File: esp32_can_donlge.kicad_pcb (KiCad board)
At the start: 4 copper layers, 86 parts, among them J1 Conn_01x02_Male, J2 DM3AT-SF-PEJM5(40), J3 DB9_Male, J4 USB_B_Micro, Q1 DMG2305UX-7, Q2 BC817, Q3 BC817, U1 ESP32-WROOM-32, U2 SN65HVD230DR, U3 TLP175A, U4 LT8607, U5 USBLC6-2SC6, U6 CP2102N-A01-GQFN24, Y1 LFXTAL009709Bulk

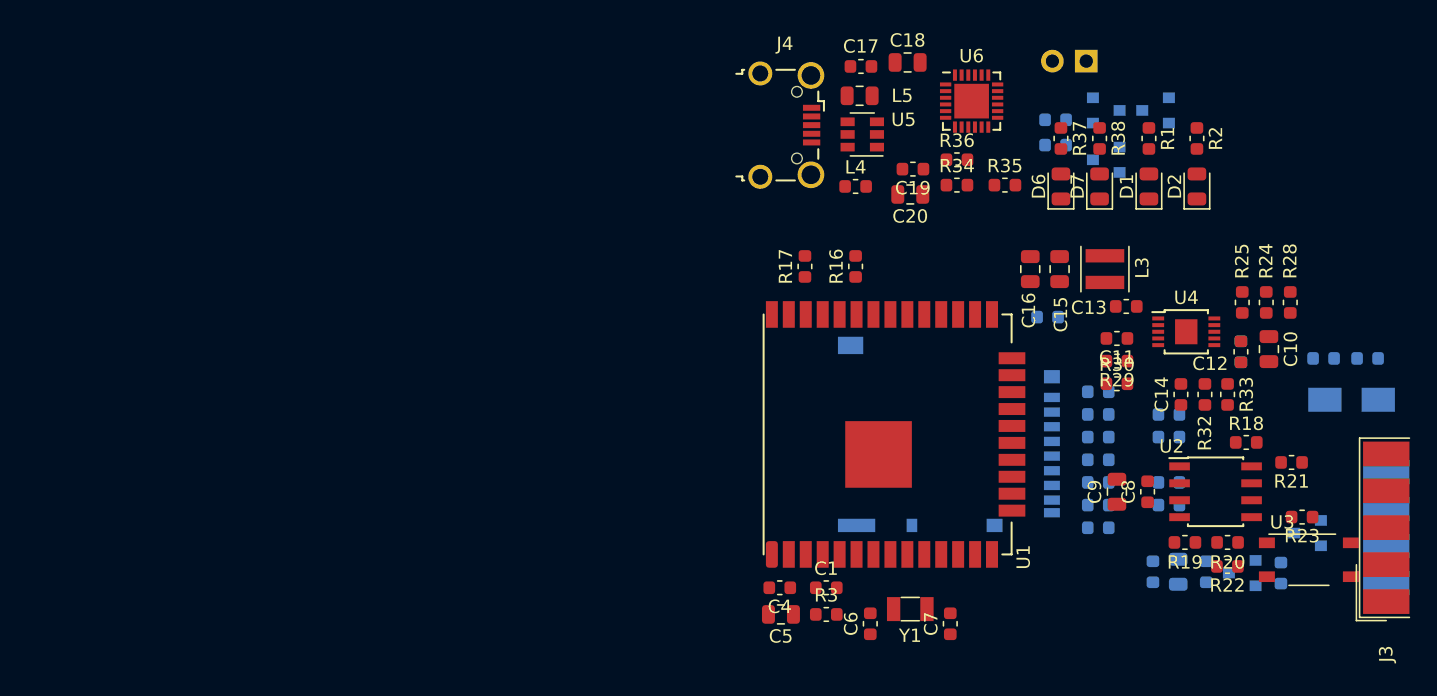
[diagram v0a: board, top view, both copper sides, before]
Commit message: changed to a more basic variant of the esp32
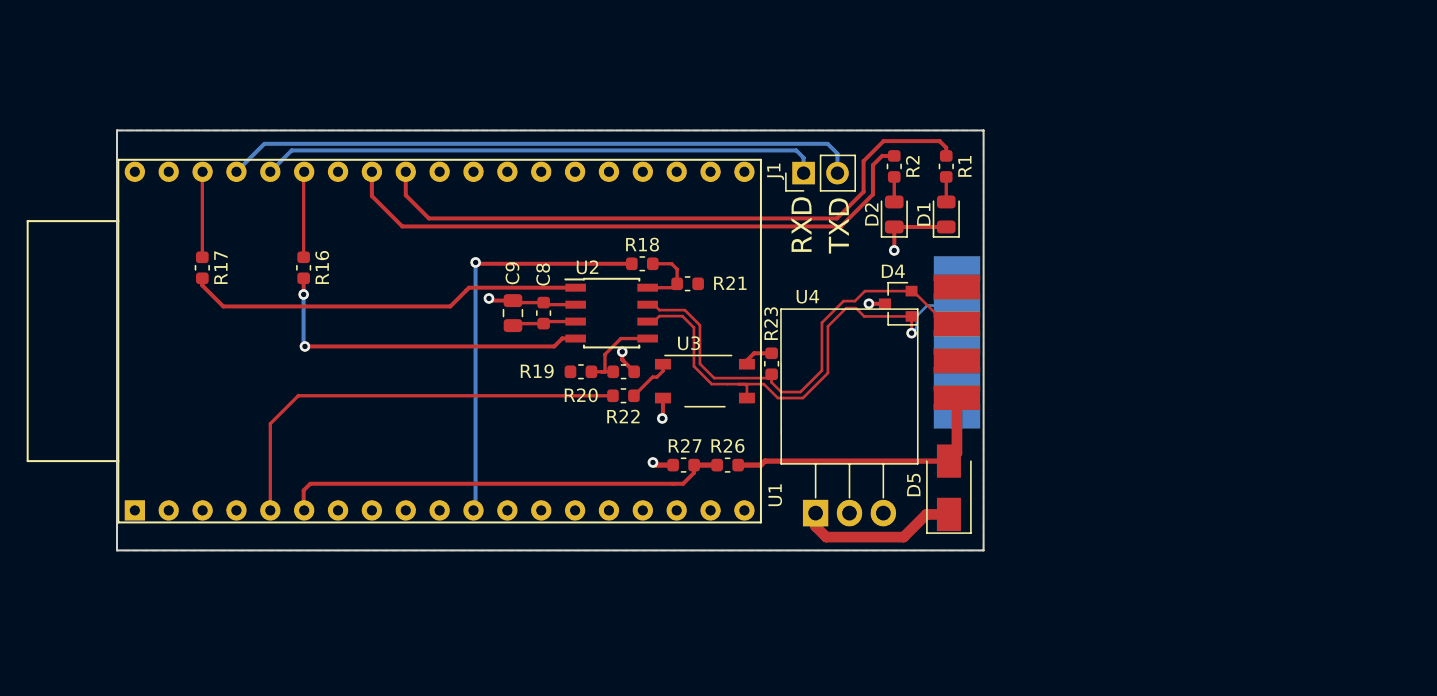
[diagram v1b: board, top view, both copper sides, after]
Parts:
- removed C1, C13, C19, C2, C4: 100n/25V, bytewerk_capacitors:C_0603_1608Metric
- removed C10, C15, C16, C3, C5: 10u/25V, bytewerk_capacitors:C_0805_2012Metric
- removed C11: 1u/25V, bytewerk_capacitors:C_0603_1608Metric
- removed C12: 10n/25V, bytewerk_capacitors:C_0603_1608Metric
- removed C14: 10p/50V, bytewerk_capacitors:C_0603_1608Metric
- removed C17: 100n/10V, bytewerk_capacitors:C_0603_1608Metric
- removed C18, C20: 4u7/10V, bytewerk_capacitors:C_0805_2012Metric
- removed C6, C7: C, bytewerk_capacitors:C_0603_1608Metric
- removed D3: BAT54C, Package_TO_SOT_SMD:SOT-23
- removed D6, D7: LED, LED_SMD:LED_0805_2012Metric
- removed J2: DM3AT-SF-PEJM5(40), Connector_Card:microSD_HC_Hirose_DM3AT-SF-PEJM5
- removed J4: USB_B_Micro, Connector_USB:USB_Micro-B_Wuerth_629105150521_CircularHoles
- removed L1, L2, L4: L, Inductor_SMD:L_0603_1608Metric
- removed L3: XFL3012-222ME, bytewerk-inductors:L_Coilcraft_XLF3012
- removed L5: L, Inductor_SMD:L_0805_2012Metric
- removed Q1: DMG2305UX-7, Package_TO_SOT_SMD:SOT-23
- removed Q2, Q3: BC817, Package_TO_SOT_SMD:SOT-23
- removed R10: 10R, bytewerk_resistors:R_0603_1608Metric
- removed R11, R12, R13, R9: 33R, bytewerk_resistors:R_0603_1608Metric
- removed R14, R30: 200R, bytewerk_resistors:R_0603_1608Metric
- removed R15, R3, R4, R5, R6, R7, R8: 10k, bytewerk_resistors:R_0603_1608Metric
- removed R24, R32: 1M, bytewerk_resistors:R_0603_1608Metric
- removed R25: 120k, bytewerk_resistors:R_0603_1608Metric
- removed R28: n.b., bytewerk_resistors:R_0603_1608Metric
- removed R29: 18k, bytewerk_resistors:R_0603_1608Metric
- removed R31: 82k, bytewerk_resistors:R_0603_1608Metric
- removed R33: 309k, bytewerk_resistors:R_0603_1608Metric
- removed R34: 22k, bytewerk_resistors:R_0603_1608Metric
- removed R35: 47k, bytewerk_resistors:R_0603_1608Metric
- removed R36, R37, R38, R39, R40: 1k, bytewerk_resistors:R_0603_1608Metric
- removed U5: USBLC6-2SC6, Package_TO_SOT_SMD:SOT-23-6
- removed U6: CP2102N-A01-GQFN24, Package_DFN_QFN:QFN-24-1EP_4x4mm_P0.5mm_EP2.6x2.6mm
- removed Y1: LFXTAL009709Bulk, Crystal:Crystal_SMD_3215-2Pin_3.2x1.5mm
- D4, D5, R26, R27: moved to F.Cu
- J1: footprint Connector_PinHeader_2.54mm:PinHeader_1x02_P2.54mm_Horizontal -> Connector_PinHeader_2.54mm:PinHeader_1x02_P2.54mm_Vertical; moved to F.Cu
- J3: moved to B.Cu
- U1: value ESP32-WROOM-32 -> ESP32-DevKitC-32D; footprint bytewerk-esp32:ESP32-WROOM-32 -> bytewerk-esp32:ESP32-DevKitC-32D
- U4: value LT8607 -> OKI-78SR; footprint Package_SO:MSOP-10-1EP_3x3mm_P0.5mm_EP1.68x1.88mm -> bytewerk-TO-packages:TO-220-3_Horizontal_TabDown
- moved R26 48.7 mm to (157.0, 94.6)
- moved R27 48.7 mm to (153.7, 94.6)
- moved R18 47.2 mm to (150.6, 79.5)
- moved R21 47.2 mm to (154.0, 81.0)
- moved C8 47.2 mm to (143.2, 83.2)
- moved U3 47.2 mm to (155.3, 88.3)
- moved C9 47.2 mm to (140.9, 83.2)
- moved U2 47.2 mm to (148.3, 83.2)
- moved R19 47.1 mm to (146.0, 87.6)
- moved R20 47.1 mm to (149.2, 87.6)
- moved R22 47.1 mm to (149.2, 89.4)
- moved R17 45.2 mm to (117.6, 79.8), turned to 270 degrees
- moved R23 41.4 mm to (160.3, 87.0), turned to 90 degrees
- moved R16 41.4 mm to (125.2, 79.8), turned to 270 degrees
- moved D4 35.2 mm to (169.8, 82.5)
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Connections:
- J1 pad 1: /esp32/BOOT -> /esp32/RXD
- J1 pad 2: GND -> /esp32/TXD
- U1 pad 1: GND -> +3V3
- U1 pad 10: /esp32/DET_B -> (no net)
- U1 pad 11: /esp32/SD_EN -> /can_interface/CAN_EN
- U1 pad 12: /can_interface/CAN_EN -> (no net)
- U1 pad 13: /esp32/SD_CLK -> (no net)
- U1 pad 14: /esp32/SD_DAT2 -> GND
- U1 pad 15: GND -> (no net)
- U1 pad 16: /esp32/SD_DAT3 -> (no net)
- U1 pad 2: +3V3 -> (no net)
- U1 pad 20: (no net) -> GND
- U1 pad 22: (no net) -> Net-(R17-Pad1)
- U1 pad 23: /esp32/SD_CMD -> /esp32/TXD
- U1 pad 24: /esp32/SD_DAT0 -> /esp32/RXD
- U1 pad 25: /esp32/BOOT -> Net-(R16-Pad1)
- U1 pad 26: /esp32/SD_DAT1 -> GND
- U1 pad 27: /esp32/DET_A -> /esp32/TEST_LED1
- U1 pad 28: /esp32/DET_B -> /esp32/TEST_LED0
- U1 pad 3: /esp32/ESP_EN -> (no net)
- U1 pad 30: /esp32/TEST_LED0 -> (no net)
- U1 pad 31: /esp32/TEST_LED1 -> (no net)
- U1 pad 33: Net-(R16-Pad1) -> (no net)
- U1 pad 34: /usb_uart/TXD -> (no net)
- U1 pad 35: /usb_uart/RXD -> (no net)
- U1 pad 36: Net-(R17-Pad1) -> (no net)
- U1 pad 37: /esp32/DET_A -> (no net)
- U1 pad 38: GND -> (no net)
- U1 pad 5: (no net) -> /can_interface/CAN_TERM_EN
- U1 pad 6: /can_interface/CAN_TERM_EN -> BAT_ADC_IN
- U1 pad 7: BAT_ADC_IN -> (no net)
- U1 pad 8: Net-(C6-Pad2) -> (no net)
- U1 pad 9: Net-(C7-Pad2) -> (no net)
- U4 pad 1: Net-(C13-Pad1) -> +12V
- U4 pad 2: Net-(C13-Pad2) -> GND
- U4 pad 3: Net-(C11-Pad1) -> +3V3
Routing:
- net /esp32/TXD: track 0.00 -> 47.7 mm
- net /esp32/TEST_LED0: track 0.00 -> 47.6 mm
- net /esp32/TEST_LED1: track 0.00 -> 45.4 mm
- net /esp32/RXD: track 0.00 -> 42.0 mm
- net /can_interface/CAN_N: track 0.00 -> 37.0 mm, vias 0 -> 1
- net /can_interface/CAN_P: track 0.00 -> 34.5 mm
- net BAT_ADC_IN: track 0.00 -> 33.7 mm
- net /can_interface/CAN_TERM_EN: track 0.00 -> 33.1 mm
- net /can_interface/CAN_EN: track 0.00 -> 30.4 mm, vias 0 -> 1
- net /can_interface/CAN_TX: track 0.00 -> 29.8 mm
- net /can_interface/CAN_RX: track 0.00 -> 25.7 mm, vias 0 -> 2
- net /power_supply/V_BAT: track 0.00 -> 21.3 mm
- net GND: track 0.00 -> 18.6 mm, vias 0 -> 6
- net +12V: track 0.00 -> 12.0 mm
- net Net-(R19-Pad2): track 0.00 -> 6.88 mm
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- added copper zone on F.Cu, net +3V3
- added copper zone on B.Cu, net GND
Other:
- board outline added: 65 x 31.5 mm
- copper layers 4 -> 2
- rule pad_to_mask_clearance: 0.2 -> 0.15
- board text added: "RXD"
- board text added: "TXD"

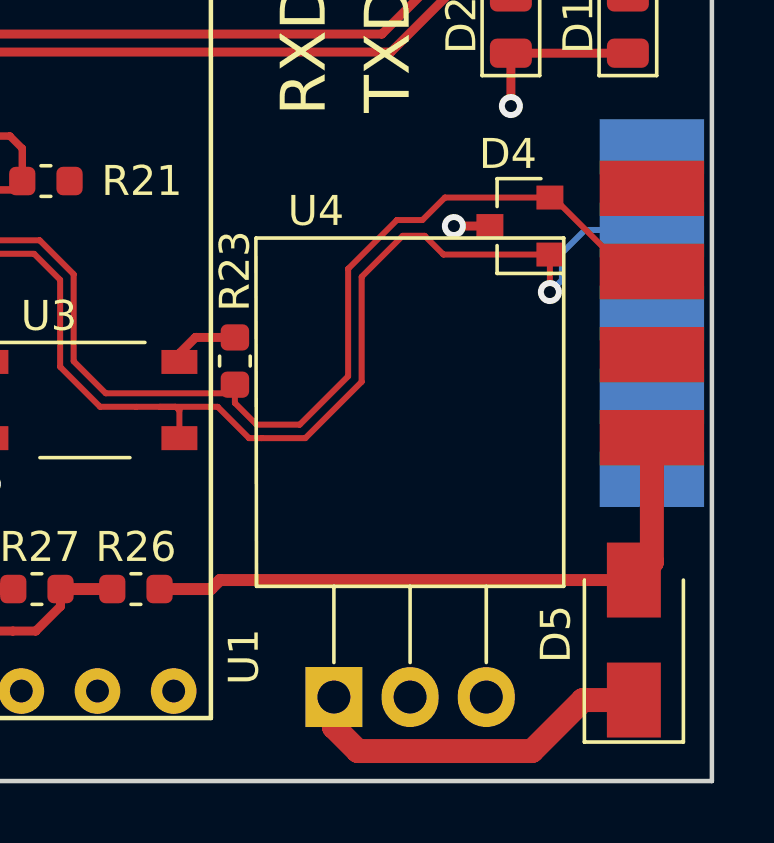
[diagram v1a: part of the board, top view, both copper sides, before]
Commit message: minor changes in schematic, fixed wrong footprint of voltage regulator
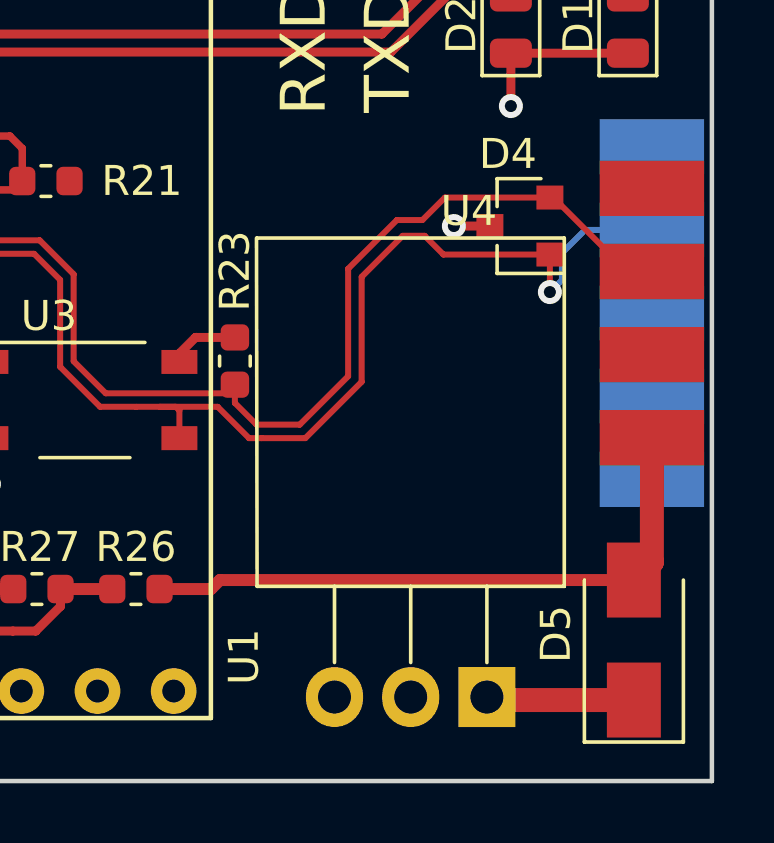
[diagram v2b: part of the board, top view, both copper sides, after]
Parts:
- moved U4 5.10 mm to (168.7, 98.2)
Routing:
- net +12V: track 12.0 -> 5.14 mm
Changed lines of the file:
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@@
     (thickness 1.6)
     (drawings 6)
-    (tracks 166)
+    (tracks 164)
     (zones 0)
     (modules 24)
@@
   )
   (setup
-    (last_trace_width 0.4)
+    (last_trace_width 0.25)
     (user_trace_width 0.2)
     (user_trace_width 0.3)
@@
     (add_net "Net-(R22-Pad1)")
     (add_net "Net-(R23-Pad2)")
+  )
+  (module bytewerk-TO-packages:TO-220-3_Horizontal_TabDown (layer F.Cu)
+    (at 168.7 98.2)
+    (descr "TO-220-3, Horizontal, RM 2.54mm, see https://www.vishay.com/docs/66542/to-220-1.pdf")
+    (tags "TO-220-3 Horizontal RM 2.54mm")
+    (fp_text reference U4 (at -0.6 -16.2) (layer F.SilkS)
+      (effects (font (size 1 1) (thickness 0.15)))
+    )
+    (fp_text value OKI-78SR (at 2.54 2) (layer F.Fab)
+      (effects (font (size 1 1) (thickness 0.15)))
+    )
+    (fp_text user %R (at -2.58 -9) (layer F.Fab)
+      (effects (font (size 1 1) (thickness 0.15)))
+    )
+    (fp_line (start 2.71 -15.5) (end -7.79 -15.5) (layer F.CrtYd) (width 0.05))
+    (fp_line (start 2.71 1.25) (end 2.71 -15.5) (layer F.CrtYd) (width 0.05))
+    (fp_line (start -7.79 1.25) (end 2.71 1.25) (layer F.CrtYd) (width 0.05))
+    (fp_line (start -7.79 -15.5) (end -7.79 1.25) (layer F.CrtYd) (width 0.05))
+    (fp_line (start 0 -3.69) (end 0 -1.15) (layer F.SilkS) (width 0.12))
+    (fp_line (start -2.54 -3.69) (end -2.54 -1.15) (layer F.SilkS) (width 0.12))
+    (fp_line (start -5.08 -3.69) (end -5.08 -1.15) (layer F.SilkS) (width 0.12))
+    (fp_line (start 2.58 -15.3) (end 2.58 -3.69) (layer F.SilkS) (width 0.12))
+    (fp_line (start -7.68 -15.3) (end -7.66 -3.69) (layer F.SilkS) (width 0.12))
+    (fp_line (start -7.66 -15.3) (end 2.58 -15.3) (layer F.SilkS) (width 0.12))
+    (fp_line (start -7.66 -3.69) (end 2.58 -3.69) (layer F.SilkS) (width 0.12))
+    (fp_line (start 0 -3.81) (end 0 0) (layer F.Fab) (width 0.1))
+    (fp_line (start -2.54 -3.81) (end -2.54 0) (layer F.Fab) (width 0.1))
+    (fp_line (start -5.08 -3.81) (end -5.08 0) (layer F.Fab) (width 0.1))
+    (fp_line (start 2.46 -3.81) (end -7.54 -3.81) (layer F.Fab) (width 0.1))
+    (fp_line (start 2.46 -13.06) (end 2.46 -3.81) (layer F.Fab) (width 0.1))
+    (fp_line (start -7.54 -13.06) (end 2.46 -13.06) (layer F.Fab) (width 0.1))
+    (fp_line (start -7.54 -3.81) (end -7.54 -13.06) (layer F.Fab) (width 0.1))
+    (fp_line (start 2.46 -13.06) (end -7.54 -13.06) (layer F.Fab) (width 0.1))
+    (pad 1 thru_hole rect (at 0 0) (size 1.905 2) (drill 1.1) (layers *.Cu *.Mask)
+      (net 3 +12V))
+    (pad 2 thru_hole oval (at -2.54 0) (size 1.905 2) (drill 1.1) (layers *.Cu *.Mask)
+      (net 1 GND))
+    (pad 3 thru_hole oval (at -5.08 0) (size 1.905 2) (drill 1.1) (layers *.Cu *.Mask)
+      (net 2 +3V3))
+    (model ${MYOWN3DMOD}/Regulators/mps_dcdc_oki_78sr_horiz_a.step
+      (offset (xyz 3 0.55 7.5))
+      (scale (xyz 1 1 1))
+      (rotate (xyz 180 0 180))
+    )
   )
   (module bytewerk_capacitors:C_0603_1608Metric (layer F.Cu)
@@
     (pad 38 thru_hole circle (at 22.86 -12.7) (size 1.524 1.524) (drill 0.762) (layers *.Cu *.Mask))
   )
-  (module bytewerk-TO-packages:TO-220-3_Horizontal_TabDown (layer F.Cu)
-    (at 163.6 98.2)
-    (descr "TO-220-3, Horizontal, RM 2.54mm, see https://www.vishay.com/docs/66542/to-220-1.pdf")
-    (tags "TO-220-3 Horizontal RM 2.54mm")
-    (fp_text reference U4 (at -0.6 -16.2) (layer F.SilkS)
-      (effects (font (size 1 1) (thickness 0.15)))
-    )
-    (fp_text value OKI-78SR (at 2.54 2) (layer F.Fab)
-      (effects (font (size 1 1) (thickness 0.15)))
-    )
-    (fp_line (start 7.54 -13.06) (end -2.46 -13.06) (layer F.Fab) (width 0.1))
-    (fp_line (start -2.46 -3.81) (end -2.46 -13.06) (layer F.Fab) (width 0.1))
-    (fp_line (start -2.46 -13.06) (end 7.54 -13.06) (layer F.Fab) (width 0.1))
-    (fp_line (start 7.54 -13.06) (end 7.54 -3.81) (layer F.Fab) (width 0.1))
-    (fp_line (start 7.54 -3.81) (end -2.46 -3.81) (layer F.Fab) (width 0.1))
-    (fp_line (start 0 -3.81) (end 0 0) (layer F.Fab) (width 0.1))
-    (fp_line (start 2.54 -3.81) (end 2.54 0) (layer F.Fab) (width 0.1))
-    (fp_line (start 5.08 -3.81) (end 5.08 0) (layer F.Fab) (width 0.1))
-    (fp_line (start -2.58 -3.69) (end 7.66 -3.69) (layer F.SilkS) (width 0.12))
-    (fp_line (start -2.58 -15.3) (end 7.66 -15.3) (layer F.SilkS) (width 0.12))
-    (fp_line (start -2.6 -15.3) (end -2.58 -3.69) (layer F.SilkS) (width 0.12))
-    (fp_line (start 7.66 -15.3) (end 7.66 -3.69) (layer F.SilkS) (width 0.12))
-    (fp_line (start 0 -3.69) (end 0 -1.15) (layer F.SilkS) (width 0.12))
-    (fp_line (start 2.54 -3.69) (end 2.54 -1.15) (layer F.SilkS) (width 0.12))
-    (fp_line (start 5.08 -3.69) (end 5.08 -1.15) (layer F.SilkS) (width 0.12))
-    (fp_line (start -2.71 -15.5) (end -2.71 1.25) (layer F.CrtYd) (width 0.05))
-    (fp_line (start -2.71 1.25) (end 7.79 1.25) (layer F.CrtYd) (width 0.05))
-    (fp_line (start 7.79 1.25) (end 7.79 -15.5) (layer F.CrtYd) (width 0.05))
-    (fp_line (start 7.79 -15.5) (end -2.71 -15.5) (layer F.CrtYd) (width 0.05))
-    (fp_text user %R (at 2.5 -9) (layer F.Fab)
-      (effects (font (size 1 1) (thickness 0.15)))
-    )
-    (pad 1 thru_hole rect (at 0 0) (size 1.905 2) (drill 1.1) (layers *.Cu *.Mask)
-      (net 3 +12V))
-    (pad 2 thru_hole oval (at 2.54 0) (size 1.905 2) (drill 1.1) (layers *.Cu *.Mask)
-      (net 1 GND))
-    (pad 3 thru_hole oval (at 5.08 0) (size 1.905 2) (drill 1.1) (layers *.Cu *.Mask)
-      (net 2 +3V3))
-    (model ${MYOWN3DMOD}/Regulators/mps_dcdc_oki_78sr_horiz_a.step
-      (offset (xyz 8.050000000000001 0.55 7.5))
-      (scale (xyz 1 1 1))
-      (rotate (xyz 180 0 180))
-    )
-  )
   (gr_text RXD (at 162.6 76.6 90) (layer F.SilkS)
     (effects (font (size 1.5 1.5) (thickness 0.3)))
@@
   (segment (start 141.05 83.9875) (end 140.9 84.1375) (width 0.25) (layer F.Cu) (net 2))
   (segment (start 143.2 83.9875) (end 141.05 83.9875) (width 0.25) (layer F.Cu) (net 2))
-  (segment (start 163.6 99.2) (end 163.6 98.2) (width 0.8) (layer F.Cu) (net 3))
-  (segment (start 164.4 100) (end 163.6 99.2) (width 0.8) (layer F.Cu) (net 3))
-  (segment (start 170.2 100) (end 164.4 100) (width 0.8) (layer F.Cu) (net 3))
-  (segment (start 173.6 98.3) (end 171.9 98.3) (width 0.8) (layer F.Cu) (net 3))
-  (segment (start 171.9 98.3) (end 170.2 100) (width 0.8) (layer F.Cu) (net 3))
+  (segment (start 168.6 98.2) (end 168.7 98.2) (width 0.8) (layer F.Cu) (net 3))
+  (segment (start 173.6 98.3) (end 168.7 98.3) (width 0.8) (layer F.Cu) (net 3))
+  (segment (start 168.7 98.3) (end 168.6 98.2) (width 0.8) (layer F.Cu) (net 3))
   (segment (start 173.4 74.8625) (end 173.4 72.9875) (width 0.25) (layer F.Cu) (net 4))
   (segment (start 169.5 74.8625) (end 169.5 72.9875) (width 0.25) (layer F.Cu) (net 5))
